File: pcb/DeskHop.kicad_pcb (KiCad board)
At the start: 2 copper layers, 66.9 x 74.5 mm, 12 parts, among them J1 Keyboard In, J2 Debug2, J3 Debug1, J4 Mouse In, U1 Pico Primary, U2 Pico Secondary, U4 ADuM1201BR

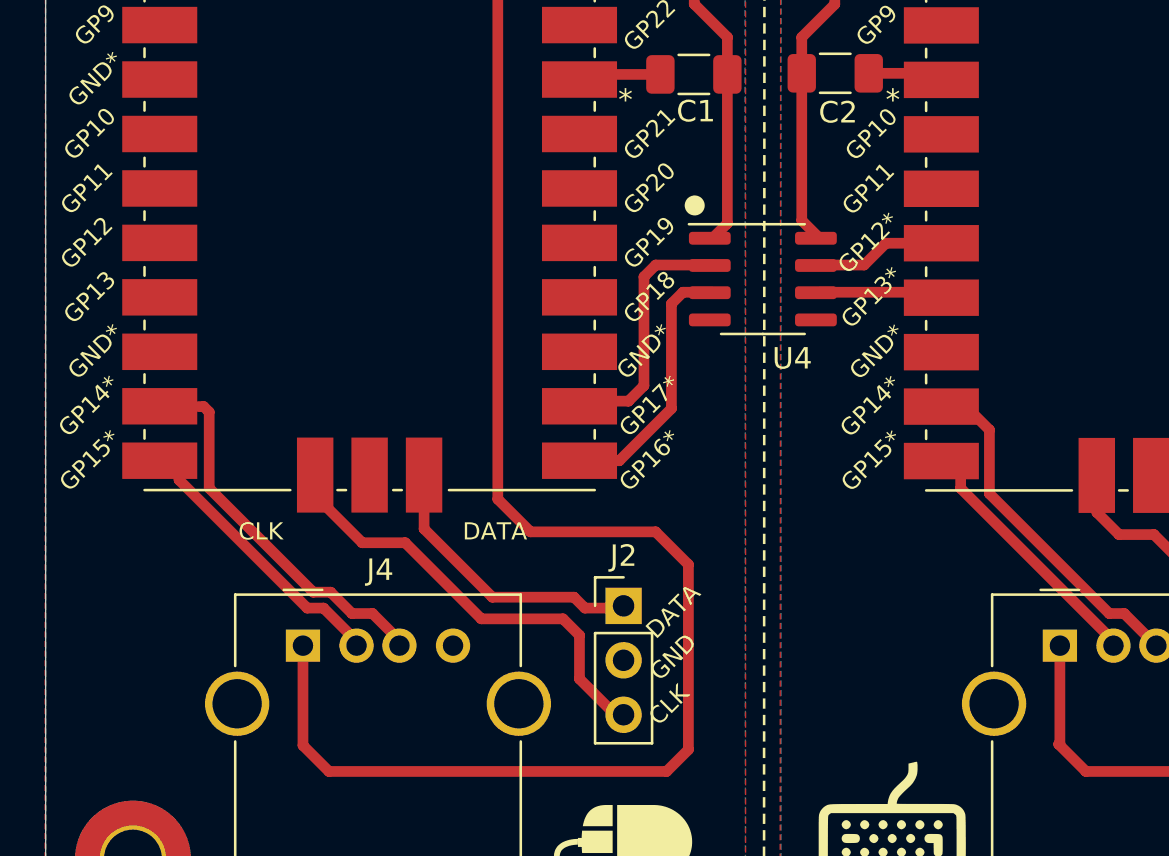
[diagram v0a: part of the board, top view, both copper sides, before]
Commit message: Add switch to PCB board
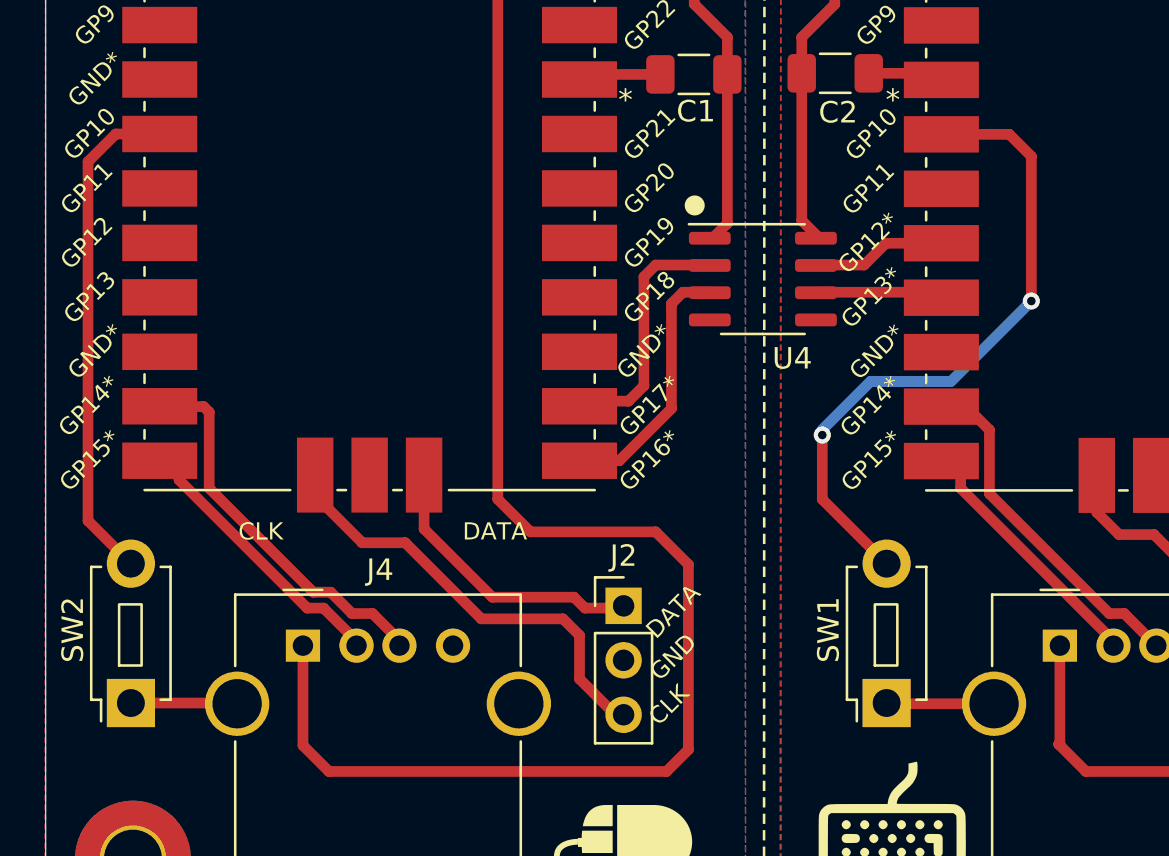
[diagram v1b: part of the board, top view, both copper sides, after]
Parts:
- added SW1: SW_Push, Button_Switch_THT:SW_PUSH_1P1T_6x3.5mm_H5.0_APEM_MJTP1250, F.Cu at (73.0, 104.2)
- added SW2: SW_Push, Button_Switch_THT:SW_PUSH_1P1T_6x3.5mm_H5.0_APEM_MJTP1250, F.Cu at (37.8, 104.2)
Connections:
- net /UART A TX renamed UART A TX
- net /UART B RX renamed UART B RX
- net /UART B TX renamed UART B TX
- net Net-(J1-VBUS) renamed VBUS1
- net Net-(J4-VBUS) renamed VBUS2
- net Net-(U2-3V3) renamed 3V3_BUS2
- U1 pad 14: unconnected-(U1-GPIO10-Pad14) -> Net-(U1-GPIO10)
- U1 pad 17: unconnected-(U1-GPIO13-Pad17) -> UART A RX
- U2 pad 14: unconnected-(U2-GPIO10-Pad14) -> Net-(U2-GPIO10)
- U4 pad 6: (no net) -> UART A RX
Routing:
- net Net-(U1-GPIO10): track 0.00 -> 30.2 mm, vias 0 -> 2
- net Net-(U2-GPIO10): track 0.00 -> 24.4 mm
- net unconnected-(U1-GPIO13-Pad17): track 6.71 -> 0.00 mm
- net UART A RX: track 0.00 -> 6.71 mm
- net GND2: track 4.41 -> 9.44 mm
- net GND: track 4.26 -> 9.23 mm
